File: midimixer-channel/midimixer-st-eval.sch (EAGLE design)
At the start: 63 parts, among them IC3 74LS595D, IC4 74165D, U1 LM1117IMPX-3.3/NOPB, Y1 8MHz 695-HCM49-8-U

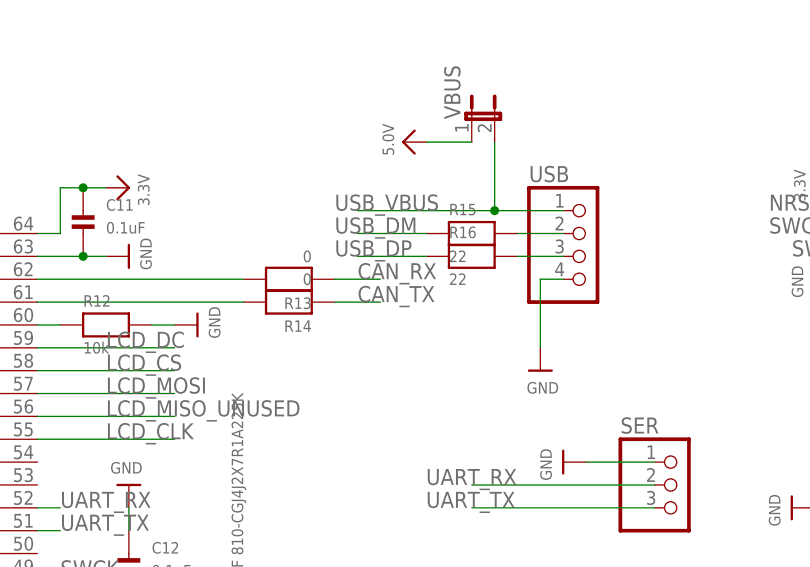
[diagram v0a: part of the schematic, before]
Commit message: fix can tx<->rx (flip them)
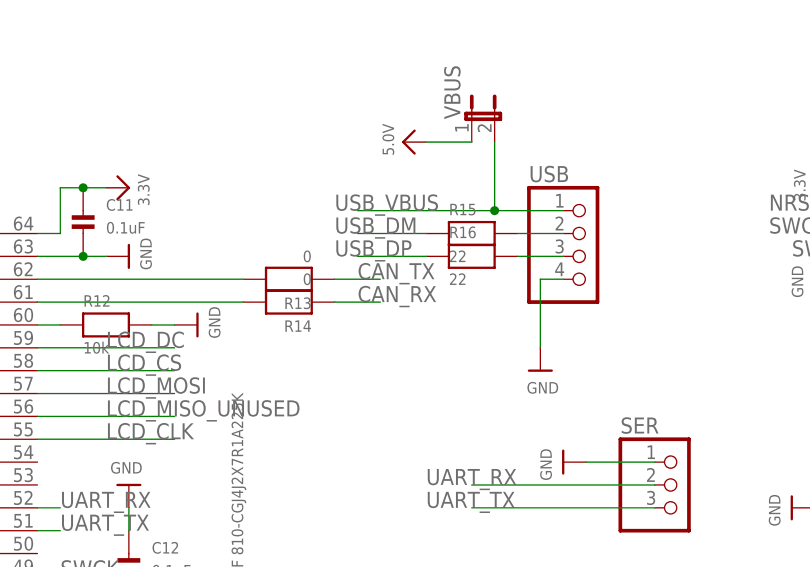
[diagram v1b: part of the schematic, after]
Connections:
- net CAN_RX: now also R14.1; no longer R13.1
- net CAN_TX: now also R13.1; no longer R14.1
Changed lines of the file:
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@@
 <?xml version="1.0" encoding="utf-8"?>
 <!DOCTYPE eagle SYSTEM "eagle.dtd">
-<eagle version="7.6.0">
+<eagle version="7.2.0">
 <drawing>
 <settings>
@@
 <net name="CAN_TX" class="0">
 <segment>
+<pinref part="D2" gate="G$1" pin="TXD"/>
+<wire x1="43.18" y1="-2.54" x2="27.94" y2="-2.54" width="0.2032" layer="91"/>
+<label x="27.94" y="-2.54" size="1.778" layer="95"/>
+</segment>
+<segment>
+<pinref part="R13" gate="G$1" pin="1"/>
+<wire x1="114.3" y1="106.68" x2="119.38" y2="106.68" width="0.2032" layer="91"/>
+<label x="116.84" y="106.68" size="1.778" layer="95"/>
+</segment>
+</net>
+<net name="CAN_RX" class="0">
+<segment>
+<pinref part="D2" gate="G$1" pin="RXD"/>
+<wire x1="43.18" y1="-7.62" x2="27.94" y2="-7.62" width="0.2032" layer="91"/>
+<label x="27.94" y="-7.62" size="1.778" layer="95"/>
+</segment>
+<segment>
 <pinref part="R14" gate="G$1" pin="1"/>
 <wire x1="114.3" y1="104.14" x2="119.38" y2="104.14" width="0.2032" layer="91"/>
 <label x="116.84" y="104.14" size="1.778" layer="95"/>
 </segment>
-<segment>
-<pinref part="D2" gate="G$1" pin="TXD"/>
-<wire x1="43.18" y1="-2.54" x2="27.94" y2="-2.54" width="0.2032" layer="91"/>
-<label x="27.94" y="-2.54" size="1.778" layer="95"/>
-</segment>
-</net>
-<net name="CAN_RX" class="0">
-<segment>
-<pinref part="D2" gate="G$1" pin="RXD"/>
-<wire x1="43.18" y1="-7.62" x2="27.94" y2="-7.62" width="0.2032" layer="91"/>
-<label x="27.94" y="-7.62" size="1.778" layer="95"/>
-</segment>
-<segment>
-<pinref part="R13" gate="G$1" pin="1"/>
-<wire x1="114.3" y1="106.68" x2="119.38" y2="106.68" width="0.2032" layer="91"/>
-<label x="116.84" y="106.68" size="1.778" layer="95"/>
-</segment>
-</net>
+</net>
